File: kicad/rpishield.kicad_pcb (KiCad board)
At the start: 2 copper layers, 64 x 55 mm, 23 parts

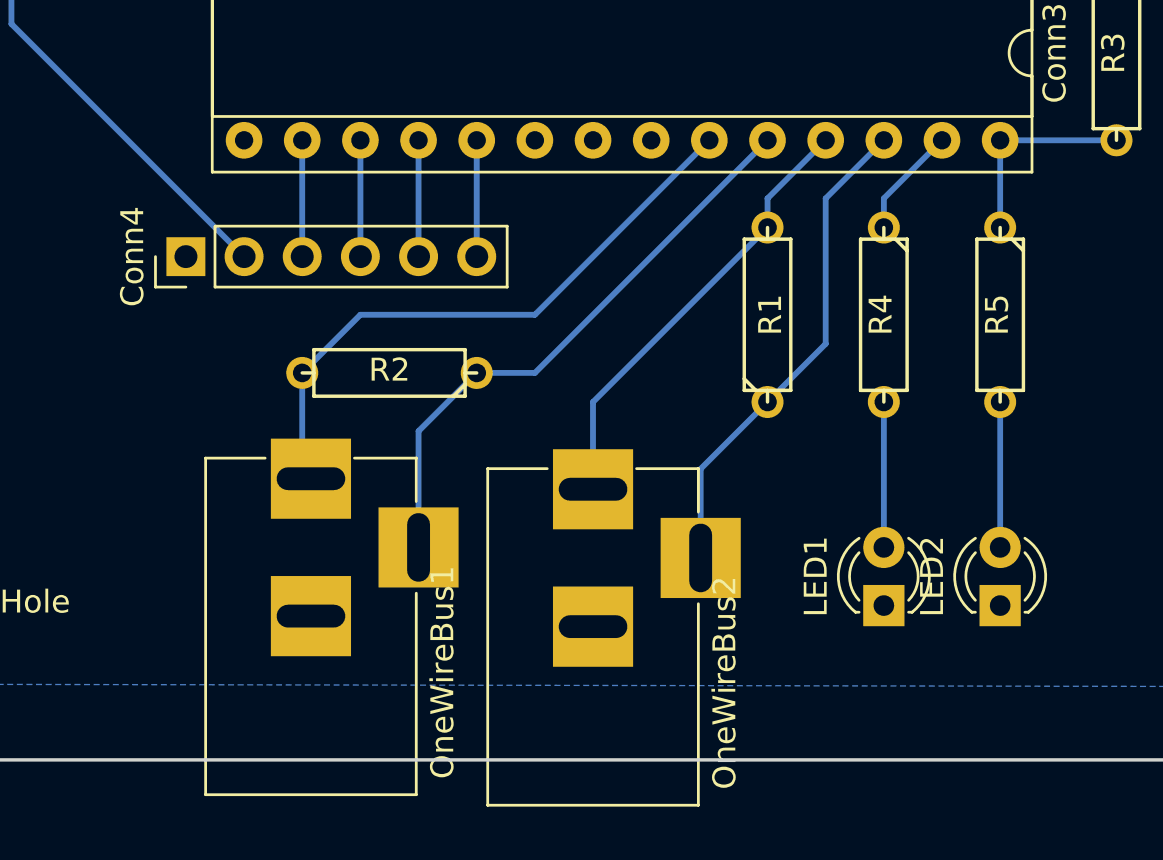
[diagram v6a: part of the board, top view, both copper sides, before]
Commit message: Better Jack track.
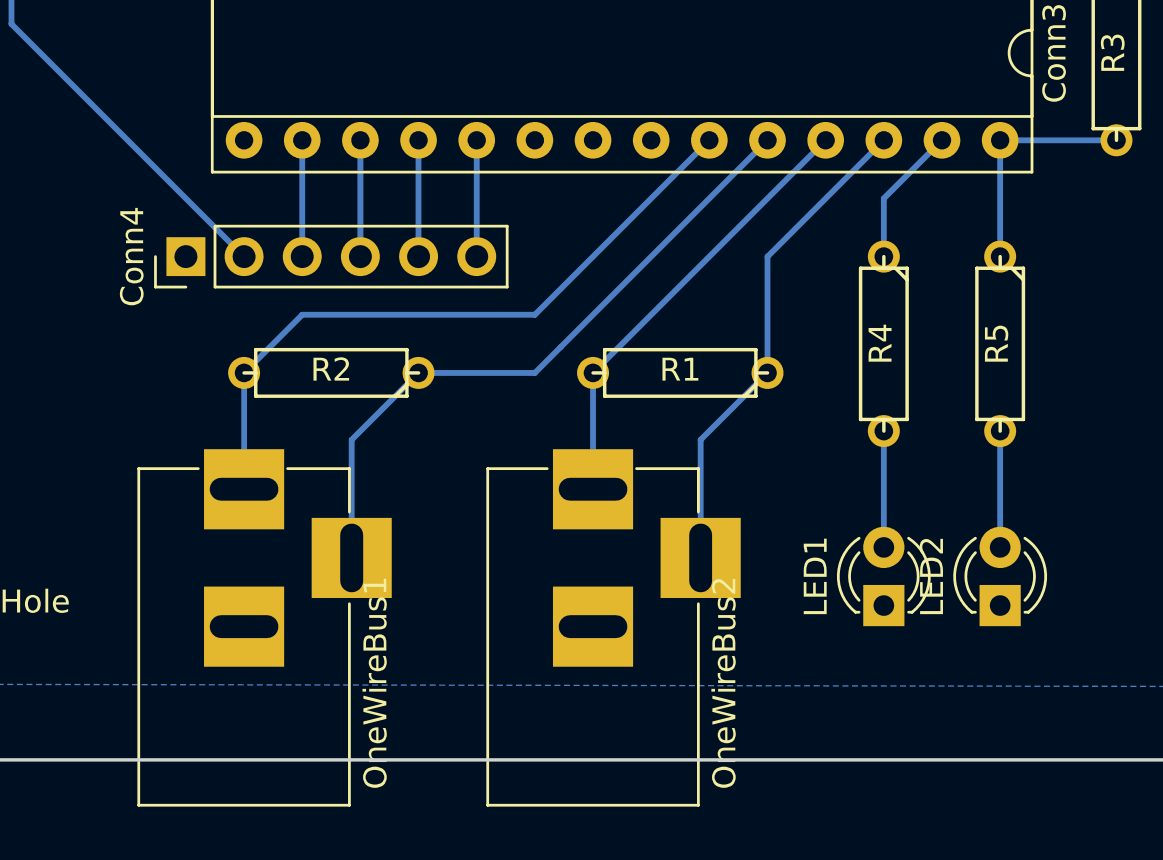
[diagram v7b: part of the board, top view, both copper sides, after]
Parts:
- moved R1 4.58 mm to (148.6, 101.6), turned to 180 degrees
- moved OneWireBus1 2.96 mm to (129.5, 106.7)
- moved R2 2.54 mm to (133.3, 101.6)
- moved R4 1.27 mm to (157.5, 100.3)
- moved R5 1.27 mm to (162.6, 100.3)
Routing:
- net /A0: track 26.1 -> 29.6 mm
- net /A1: track 25.6 -> 28.7 mm
- net Net-(LED2-Pad2): track 6.35 -> 5.08 mm
- net Net-(LED1-Pad2): track 6.35 -> 5.08 mm
- net /A5: track 8.89 -> 10.2 mm
- net /A4: track 4.86 -> 6.13 mm
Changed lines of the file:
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@@
   (general
     (links 42)
-    (no_connects 0)
+    (no_connects 9)
     (area 113.924999 63.424999 178.075001 118.575001)
     (thickness 1.6)
     (drawings 8)
-    (tracks 59)
+    (tracks 57)
     (zones 0)
     (modules 23)
@@
   )
   (module Discret:R3 (layer F.Cu)
-    (at 152.4 99.06 90)
+    (at 148.59 101.6 180)
     (descr "Resitance 3 pas")
     (tags R)
-    (fp_text reference R1 (at 0 0.127 90) (layer F.SilkS)
-      (effects (font (size 1 1) (thickness 0.15)))
-    )
-    (fp_text value 4k7 (at 0 0.127 90) (layer F.Fab)
+    (fp_text reference R1 (at 0 0.127 180) (layer F.SilkS)
+      (effects (font (size 1 1) (thickness 0.15)))
+    )
+    (fp_text value 4k7 (at 0 0.127 180) (layer F.Fab)
       (effects (font (size 1 1) (thickness 0.15)))
     )
@@
     (fp_line (start 3.302 1.016) (end 3.302 0) (layer F.SilkS) (width 0.15))
     (fp_line (start -3.302 -0.508) (end -2.794 -1.016) (layer F.SilkS) (width 0.15))
-    (pad 1 thru_hole circle (at -3.81 0 90) (size 1.397 1.397) (drill 0.8128) (layers *.Cu *.Mask)
+    (pad 1 thru_hole circle (at -3.81 0 180) (size 1.397 1.397) (drill 0.8128) (layers *.Cu *.Mask)
       (net 26 /A3))
-    (pad 2 thru_hole circle (at 3.81 0 90) (size 1.397 1.397) (drill 0.8128) (layers *.Cu *.Mask)
+    (pad 2 thru_hole circle (at 3.81 0 180) (size 1.397 1.397) (drill 0.8128) (layers *.Cu *.Mask)
       (net 22 /A2))
     (model Discret.3dshapes/R3.wrl
@@
   )
   (module Connectors:BARREL_JACK (layer F.Cu)
-    (at 132.46 106.22 90)
+    (at 129.54 106.68 90)
     (descr "DC Barrel Jack")
     (tags "Power Jack")
@@
   )
   (module Discret:R3 (layer F.Cu)
-    (at 135.89 101.6 180)
+    (at 133.35 101.6 180)
     (descr "Resitance 3 pas")
     (tags R)
@@
   )
   (module Discret:R3 (layer F.Cu)
-    (at 157.48 99.06 270)
+    (at 157.48 100.33 270)
     (descr "Resitance 3 pas")
     (tags R)
@@
   )
   (module Discret:R3 (layer F.Cu)
-    (at 162.56 99.06 270)
+    (at 162.56 100.33 270)
     (descr "Resitance 3 pas")
     (tags R)
@@
   (segment (start 132.08 96.52) (end 132.08 91.44) (width 0.254) (layer B.Cu) (net 8) (status 30))
   (segment (start 134.62 96.52) (end 134.62 91.44) (width 0.254) (layer B.Cu) (net 9) (status 30))
-  (segment (start 157.48 109.22) (end 157.48 102.87) (width 0.254) (layer B.Cu) (net 20) (status 30))
-  (segment (start 162.56 109.22) (end 162.56 102.87) (width 0.254) (layer B.Cu) (net 21) (status 30))
-  (segment (start 152.4 95.25) (end 152.4 93.98) (width 0.254) (layer B.Cu) (net 22) (status 10))
-  (segment (start 152.4 93.98) (end 154.94 91.44) (width 0.254) (layer B.Cu) (net 22) (status 20))
-  (segment (start 144.78 106.68) (end 144.78 102.87) (width 0.254) (layer B.Cu) (net 22) (status 10))
-  (segment (start 144.78 102.87) (end 152.4 95.25) (width 0.254) (layer B.Cu) (net 22) (status 20))
-  (segment (start 157.48 95.25) (end 157.48 93.98) (width 0.254) (layer B.Cu) (net 23))
-  (segment (start 157.48 93.98) (end 160.02 91.44) (width 0.254) (layer B.Cu) (net 23))
+  (segment (start 157.48 104.14) (end 157.48 109.22) (width 0.254) (layer B.Cu) (net 20))
+  (segment (start 162.56 104.14) (end 162.56 109.22) (width 0.254) (layer B.Cu) (net 21))
+  (segment (start 144.78 101.6) (end 154.94 91.44) (width 0.254) (layer B.Cu) (net 22))
+  (segment (start 144.78 106.68) (end 144.78 101.6) (width 0.254) (layer B.Cu) (net 22) (status 10))
+  (segment (start 157.48 93.98) (end 157.48 96.52) (width 0.254) (layer B.Cu) (net 23))
+  (segment (start 160.02 91.44) (end 157.48 93.98) (width 0.254) (layer B.Cu) (net 23))
+  (segment (start 162.56 91.44) (end 162.56 96.52) (width 0.254) (layer B.Cu) (net 24))
   (segment (start 162.56 91.44) (end 167.64 91.44) (width 0.254) (layer B.Cu) (net 24))
-  (segment (start 162.56 95.25) (end 162.56 91.44) (width 0.254) (layer B.Cu) (net 24) (status 30))
-  (segment (start 137.16 104.14) (end 137.16 109.22) (width 0.254) (layer B.Cu) (net 25))
-  (segment (start 139.7 101.6) (end 137.16 104.14) (width 0.254) (layer B.Cu) (net 25))
-  (segment (start 139.7 101.6) (end 142.24 101.6) (width 0.254) (layer B.Cu) (net 25))
-  (segment (start 142.24 101.6) (end 152.4 91.44) (width 0.254) (layer B.Cu) (net 25) (status 20))
-  (segment (start 152.4 102.87) (end 154.94 100.33) (width 0.254) (layer B.Cu) (net 26))
-  (segment (start 154.94 93.98) (end 157.48 91.44) (width 0.254) (layer B.Cu) (net 26))
-  (segment (start 154.94 100.33) (end 154.94 93.98) (width 0.254) (layer B.Cu) (net 26))
-  (segment (start 149.48 109.68) (end 149.48 105.79) (width 0.254) (layer B.Cu) (net 26) (status 10))
-  (segment (start 149.48 105.79) (end 152.4 102.87) (width 0.254) (layer B.Cu) (net 26) (status 20))
-  (segment (start 132.08 101.6) (end 134.62 99.06) (width 0.254) (layer B.Cu) (net 27))
-  (segment (start 134.62 99.06) (end 142.24 99.06) (width 0.254) (layer B.Cu) (net 27))
+  (segment (start 142.24 101.6) (end 143.365501 100.474499) (width 0.254) (layer B.Cu) (net 25))
+  (segment (start 143.365501 100.474499) (end 152.4 91.44) (width 0.254) (layer B.Cu) (net 25))
+  (segment (start 137.16 101.6) (end 142.24 101.6) (width 0.254) (layer B.Cu) (net 25))
+  (segment (start 134.24 109.68) (end 134.24 104.52) (width 0.254) (layer B.Cu) (net 25))
+  (segment (start 134.24 104.52) (end 137.16 101.6) (width 0.254) (layer B.Cu) (net 25))
+  (segment (start 149.48 109.68) (end 149.48 104.52) (width 0.254) (layer B.Cu) (net 26) (status 10))
+  (segment (start 149.48 104.52) (end 152.4 101.6) (width 0.254) (layer B.Cu) (net 26))
+  (segment (start 152.4 101.6) (end 152.4 96.52) (width 0.254) (layer B.Cu) (net 26))
+  (segment (start 152.4 96.52) (end 157.48 91.44) (width 0.254) (layer B.Cu) (net 26))
+  (segment (start 129.54 101.6) (end 132.08 99.06) (width 0.254) (layer B.Cu) (net 27))
+  (segment (start 132.08 99.06) (end 142.24 99.06) (width 0.254) (layer B.Cu) (net 27))
   (segment (start 142.24 99.06) (end 149.86 91.44) (width 0.254) (layer B.Cu) (net 27))
-  (segment (start 132.08 105.76) (end 132.08 101.6) (width 0.254) (layer B.Cu) (net 27))
+  (segment (start 129.54 106.68) (end 129.54 101.6) (width 0.254) (layer B.Cu) (net 27))
   (segment (start 137.16 96.52) (end 137.16 91.44) (width 0.254) (layer B.Cu) (net 28) (status 30))
   (segment (start 139.7 96.52) (end 139.7 91.44) (width 0.254) (layer B.Cu) (net 29) (status 30))
@@
     (connect_pads (clearance 0.508))
     (min_thickness 0.254)
-    (fill yes (arc_segments 16) (thermal_gap 0.508) (thermal_bridge_width 0.508))
+    (fill (arc_segments 16) (thermal_gap 0.508) (thermal_bridge_width 0.508))
     (polygon
       (pts

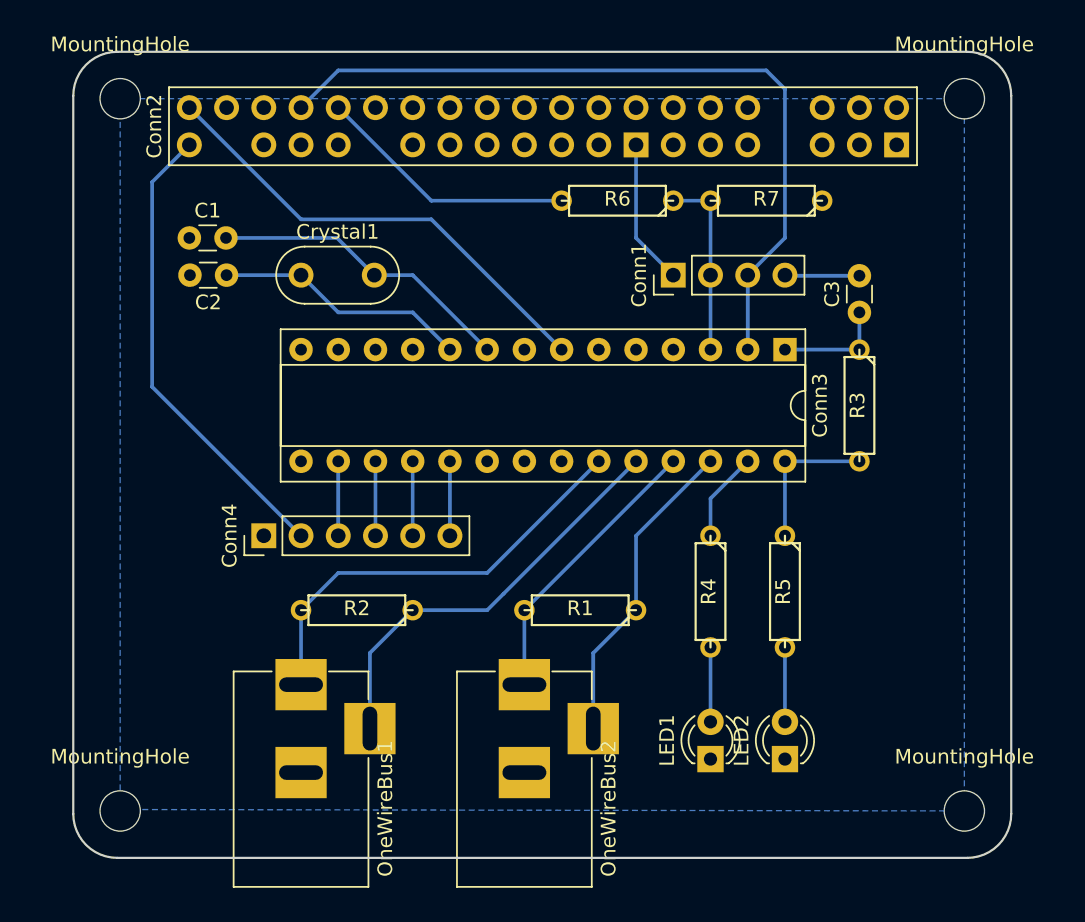
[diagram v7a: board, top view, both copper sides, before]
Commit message: SPI, LED, R, C footprint, path update.
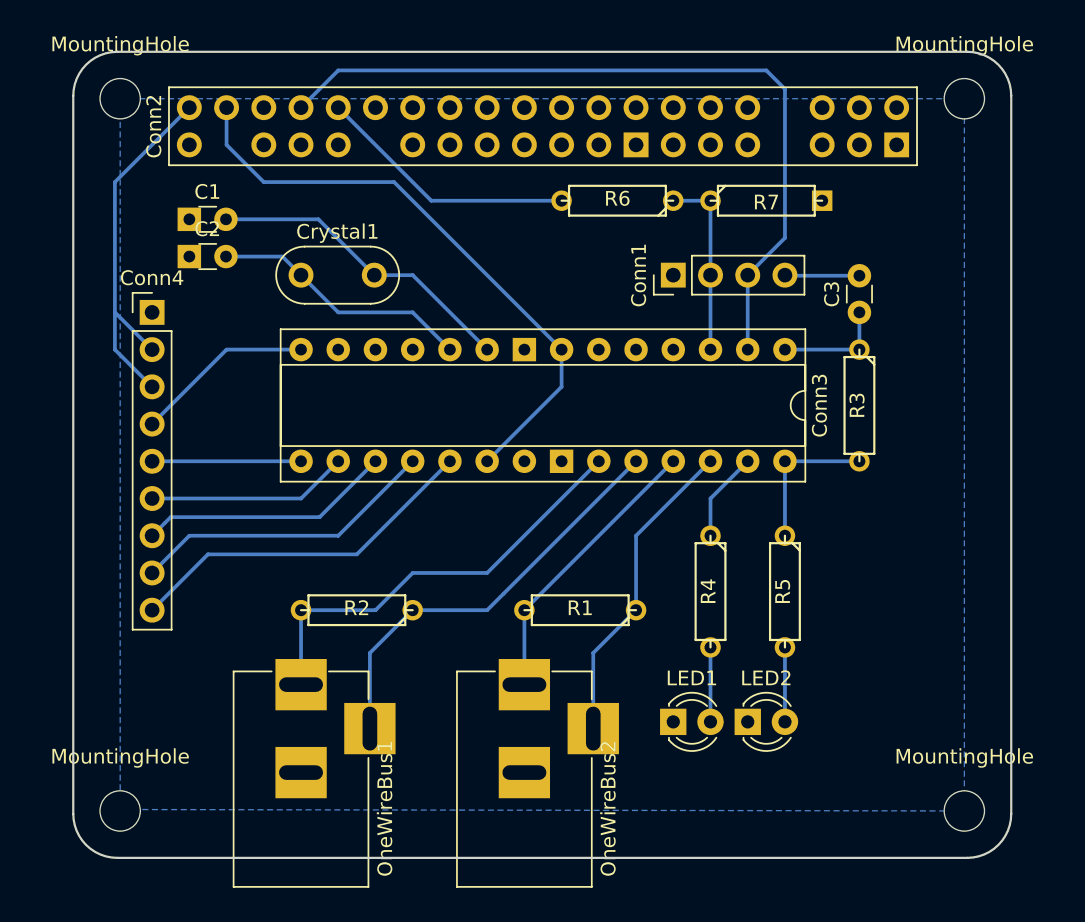
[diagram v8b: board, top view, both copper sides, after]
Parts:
- C1, C2: footprint Capacitors_THT:C_Disc_D3.0mm_W1.6mm_P2.50mm -> footprint:Custom_Disc_D3.0mm_W1.6mm_P2.50mm
- Conn2: footprint header220:Custom_Header_2x20_Pitch2.54mm -> footprint:Custom_Header_2x20_Pitch2.54mm
- Conn3: footprint Housings_DIP:DIP-28_W7.62mm_Socket -> footprint:Custom_DIP-28_W7.62mm_Socket
- Conn4: footprint Socket_Strips:Socket_Strip_Straight_1x06_Pitch2.54mm -> Socket_Strips:Socket_Strip_Straight_1x09_Pitch2.54mm
- R7: footprint Discret:R3 -> footprint:Custom_R3
- moved Conn4 17.0 mm to (119.4, 81.3), turned to 0 degrees
- moved LED1 3.59 mm to (154.9, 109.2), turned to 0 degrees
- moved LED2 3.59 mm to (160.0, 109.2), turned to 0 degrees
- moved C2 2.84 mm to (121.9, 77.5), turned to 0 degrees
- moved C1 1.27 mm to (121.9, 74.9)
- turned R7 to 0 degrees
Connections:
- C2 pad 1: /XTAL2 -> GND
- C2 pad 2: GND -> /XTAL2
- Conn1 pad 1: /GND_UART -> GND
- Conn2 pad 1: /VCC_SPI -> Net-(Conn2-Pad1)
- Conn2 pad 2: /VCC_AVR -> /VCC_LED
- Conn2 pad 25: /GND_UART -> GND
- Conn2 pad 4: Net-(Conn2-Pad4) -> /AVCC
- Conn3 pad 14: Net-(Conn3-Pad14) -> /TFT_RST
- Conn3 pad 15: Net-(Conn3-Pad15) -> /TFT_DC
- Conn3 pad 16: /D10 -> /SPI_SS
- Conn3 pad 17: /D11 -> /SPI_MISO
- Conn3 pad 18: /D12 -> /SPI_MOSI
- Conn3 pad 19: /D13 -> /SPI_SCK
- Conn3 pad 20: Net-(Conn3-Pad20) -> /AVCC
- Conn3 pad 22: Net-(Conn3-Pad22) -> GND
- Conn3 pad 7: /VCC_AVR -> /AVCC
- Conn4 pad 2: /VCC_SPI -> /VCC_LED
- Conn4 pad 3: /D10 -> /VCC_LED
- Conn4 pad 4: /D11 -> /TFT_RST
- Conn4 pad 5: /D12 -> /TFT_DC
- Conn4 pad 6: /D13 -> /SPI_SS
- R7 pad 1: GND -> /TX
- R7 pad 2: /TX -> GND
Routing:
- net /AVCC: track 0.00 -> 40.9 mm
- net /VCC_AVR: track 32.2 -> 0.00 mm
- net /VCC_SPI: track 31.9 -> 0.00 mm
- net /VCC_LED: track 0.00 -> 25.8 mm
- net /SPI_SCK: track 0.00 -> 24.5 mm
- net /SPI_MOSI: track 0.00 -> 20.9 mm
- net /SPI_MISO: track 0.00 -> 17.3 mm
- net /SPI_SS: track 0.00 -> 13.8 mm
- net /TFT_RST: track 0.00 -> 12.3 mm
- net /TFT_DC: track 0.00 -> 10.2 mm
- net /GND_UART: track 9.94 -> 0.00 mm
- net /D13: track 5.08 -> 0.00 mm
- net /D12: track 5.08 -> 0.00 mm
- net /D11: track 5.08 -> 0.00 mm
- net /D10: track 5.08 -> 0.00 mm
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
